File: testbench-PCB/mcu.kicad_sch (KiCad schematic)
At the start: 17 parts, among them J2 AVR-ISP, J3 AVR-JTAG, SW1 SW_Push, U1 ATmega2561-16A, Y1 X322516MLB4SI

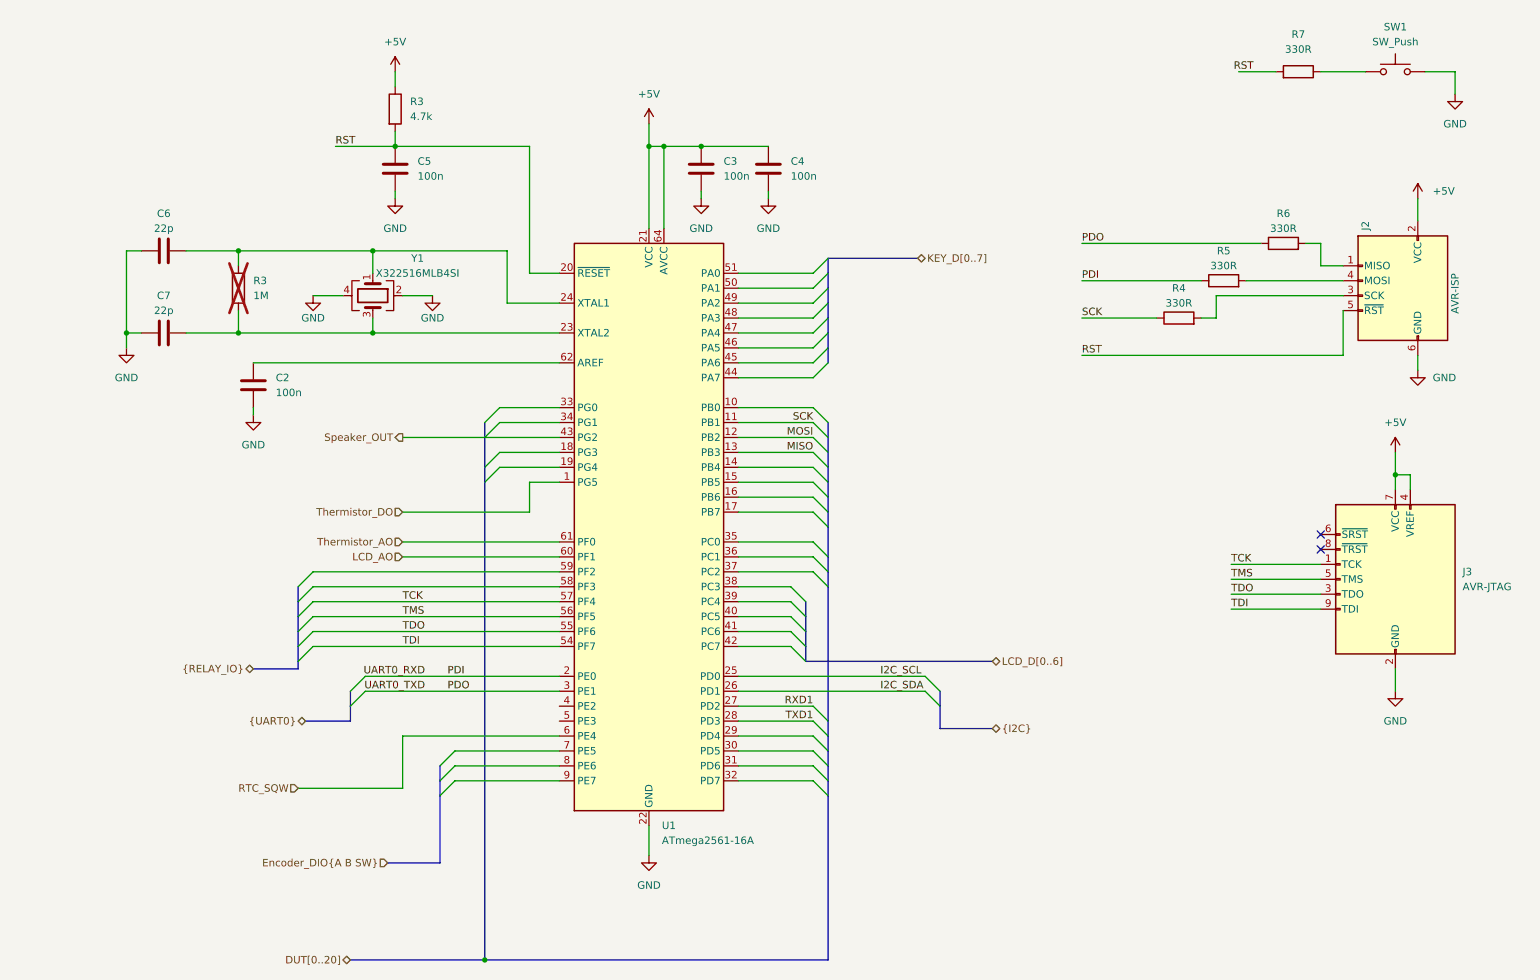
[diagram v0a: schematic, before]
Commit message: Rearanged PCB, updated footprints.
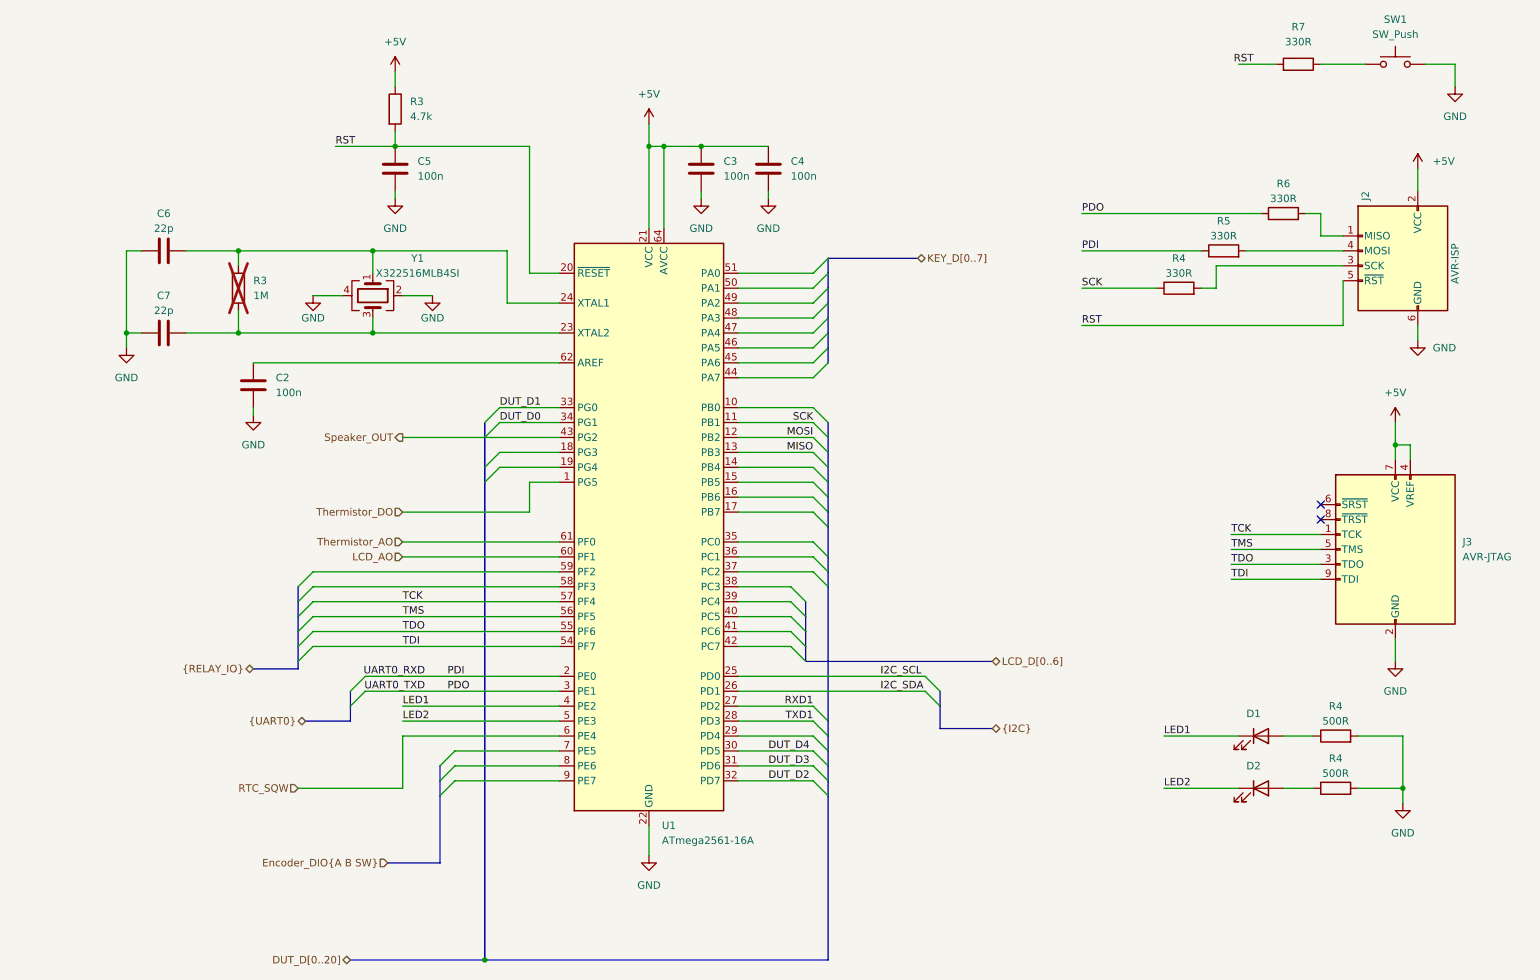
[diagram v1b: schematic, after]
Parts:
- added D1, D2: LED, LED_SMD:LED_0805_2012Metric, symbol Device:LED
- added R4 (x2): 500R, Resistor_SMD:R_0805_2012Metric, symbol Device:R
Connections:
- net GND: now also R4.2, R4.2
- net DUT_D4: now reaches U1.30 (PD5)
- net DUT_D3: now reaches U1.31 (PD6)
- net DUT_D2: now reaches U1.32 (PD7)
- net DUT_D1: now reaches U1.33 (PG0)
- net DUT_D0: now reaches U1.34 (PG1)
- net LED1: now reaches U1.4 (PE2)
- net LED1: now also D1.1 (K)
- net LED2: now reaches U1.5 (PE3)
- net LED2: now also D2.1 (K)
- new net: D1.2 (A), R4.1
- new net: D2.2 (A), R4.1
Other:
- moved on the sheet: J2, J3, R4, R5, R6, R7, SW1

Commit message: Routing the PCB.
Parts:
- removed D1: LED, LED_SMD:LED_0805_2012Metric, symbol Device:LED
- removed R4: 500R, Resistor_SMD:R_0805_2012Metric, symbol Device:R
- added C4: 100n, Capacitor_SMD:C_0805_2012Metric, symbol Device:C
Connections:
- net LED1 is gone; now on net Speaker_OUT: U1.4 (PE2)
- net +5V: now also C4.1
- net DUT_D0: now also U1.37 (PC2); no longer U1.34 (PG1)
- net DUT_D1: now also U1.36 (PC1); no longer U1.33 (PG0)
- net DUT_D2: now also U1.35 (PC0); no longer U1.32 (PD7)
- net DUT_D3: now also U1.34 (PG1); no longer U1.31 (PD6)
- net DUT_D4: now also U1.33 (PG0); no longer U1.30 (PD5)
- net GND: now also C4.2
- net LED2: now also D2.2 (A); no longer D2.1 (K), U1.5 (PE3)
- net Speaker_OUT: no longer U1.43 (PG2)
- net at R4.1: now also D2.1 (K); no longer D2.2 (A)
- net DUT_D17: now reaches U1.10 (PB0)
- net DUT_D16: now reaches U1.14 (PB4)
- net DUT_D15: now reaches U1.15 (PB5)
- net DUT_D14: now reaches U1.16 (PB6)
- net DUT_D13: now reaches U1.17 (PB7)
- net DUT_D12: now reaches U1.18 (PG3)
- net DUT_D11: now reaches U1.19 (PG4)
- net DUT_D9: now reaches U1.29 (PD4)
- net LCD_D0: now reaches U1.38 (PC3)
- net LCD_D1: now reaches U1.39 (PC4)
- net LCD_D2: now reaches U1.40 (PC5)
- net LCD_D3: now reaches U1.41 (PC6)
- net LCD_D4: now reaches U1.42 (PC7)
- net KEY_D0: now reaches U1.44 (PA7)
- net KEY_D1: now reaches U1.45 (PA6)
- net KEY_D2: now reaches U1.46 (PA5)
- net KEY_D3: now reaches U1.47 (PA4)
- net KEY_D4: now reaches U1.48 (PA3)
- net KEY_D5: now reaches U1.49 (PA2)
- net KEY_D6: now reaches U1.50 (PA1)
- net KEY_D7: now reaches U1.51 (PA0)
- net K1-IN: now reaches U1.58 (PF3)
- net K2-IN: now reaches U1.59 (PF2)
- net ENC.A: now reaches U1.7 (PE5)
- net ENC.B: now reaches U1.8 (PE6)
- net ENC.SW: now reaches U1.9 (PE7)
- net MISO renamed DUT_D18
- net MOSI renamed DUT_D19
- net RXD1 renamed DUT_D8
- net SCK renamed DUT_D20
- net TCK renamed K2-NC
- net TDI renamed K2-NO
- net TDO renamed K1-NO
- net TMS renamed K1-NC
- net TXD1 renamed DUT_D7
- new net DUT_D10: U1.30 (PD5)
- new net DUT_D5: U1.32 (PD7)
- new net DUT_D6: U1.31 (PD6)
- new net LCD_D5: U1.43 (PG2)
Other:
- moved on the sheet: C4, D2

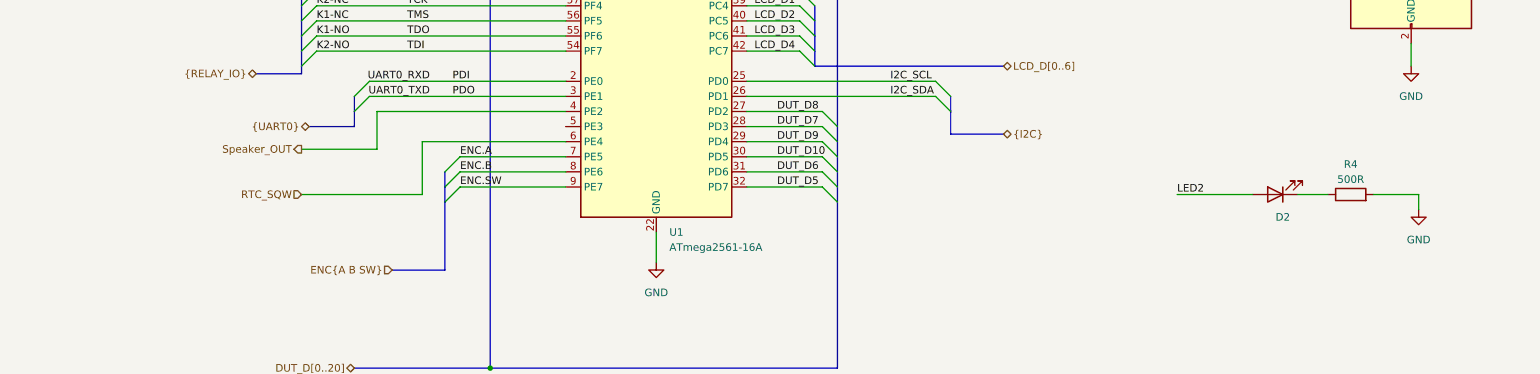
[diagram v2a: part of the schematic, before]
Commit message: Finished PCB routing, added ground plane.
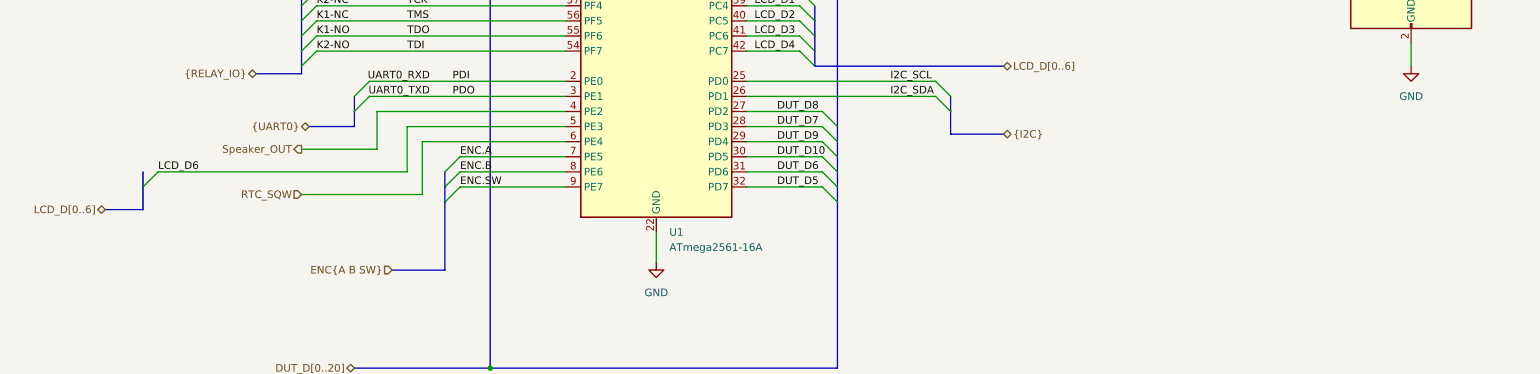
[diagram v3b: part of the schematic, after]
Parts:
- removed D2: LED, LED_SMD:LED_0805_2012Metric, symbol Device:LED
- removed R4: 500R, Resistor_SMD:R_0805_2012Metric, symbol Device:R
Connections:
- net LCD_D6: now reaches U1.5 (PE3)
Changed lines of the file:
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@@
+    (stroke (width 0) (type default))
+  )
+  (bus_entry (at 41.91 153.67) (size 2.54 -2.54)
     (stroke (width 0) (type default))
   )
@@
     (stroke (width 0) (type default))
   )
+  (wire (pts (xy 86.36 143.51) (xy 86.36 151.13))
+    (stroke (width 0) (type default))
+  )
   (wire (pts (xy 104.14 63.5) (xy 81.28 63.5))
     (stroke (width 0) (type default))
@@
     (stroke (width 0) (type default))
   )
+  (wire (pts (xy 113.03 143.51) (xy 86.36 143.51))
+    (stroke (width 0) (type default))
+  )
   (bus (pts (xy 158.75 115.57) (xy 158.75 118.11))
     (stroke (width 0) (type default))
@@
     (stroke (width 0) (type default))
   )
-  (wire (pts (xy 248.92 154.94) (xy 256.54 154.94))
-    (stroke (width 0) (type default))
-  )
   (bus (pts (xy 68.58 128.27) (xy 68.58 130.81))
     (stroke (width 0) (type default))
@@
     (stroke (width 0) (type default))
   )
+  (bus (pts (xy 41.91 153.67) (xy 41.91 157.48))
+    (stroke (width 0) (type default))
+  )
   (wire (pts (xy 259.08 78.74) (xy 259.08 76.2))
     (stroke (width 0) (type default))
@@
     (stroke (width 0) (type default))
   )
-  (wire (pts (xy 256.54 154.94) (xy 256.54 157.48))
-    (stroke (width 0) (type default))
-  )
   (wire (pts (xy 60.96 90.17) (xy 60.96 91.44))
     (stroke (width 0) (type default))
@@
     (stroke (width 0) (type default))
   )
-  (wire (pts (xy 236.22 154.94) (xy 241.3 154.94))
-    (stroke (width 0) (type default))
-  )
   (bus (pts (xy 68.58 125.73) (xy 68.58 128.27))
     (stroke (width 0) (type default))
@@
     (stroke (width 0) (type default))
   )
+  (wire (pts (xy 44.45 151.13) (xy 86.36 151.13))
+    (stroke (width 0) (type default))
+  )
   (bus (pts (xy 88.9 97.79) (xy 88.9 101.6))
     (stroke (width 0) (type default))
@@
     (stroke (width 0) (type default))
   )
+  (bus (pts (xy 41.91 151.13) (xy 41.91 153.67))
+    (stroke (width 0) (type default))
+  )
   (wire (pts (xy 100.33 95.25) (xy 113.03 95.25))
     (stroke (width 0) (type default))
@@
     (stroke (width 0) (type default))
   )
-  (wire (pts (xy 215.9 154.94) (xy 228.6 154.94))
-    (stroke (width 0) (type default))
-  )
   (bus (pts (xy 100.33 95.25) (xy 100.33 100.33))
     (stroke (width 0) (type default))
@@
     (stroke (width 0) (type default))
   )
+  (bus (pts (xy 35.56 157.48) (xy 41.91 157.48))
+    (stroke (width 0) (type default))
+  )
   (bus (pts (xy 158.75 153.67) (xy 158.75 156.21))
     (stroke (width 0) (type default))
@@
   )
   (label "TDO" (at 227.33 116.84 0) (fields_autoplaced)
+    (effects (font (size 1.27 1.27)) (justify left bottom))
+  )
+  (label "LCD_D6" (at 44.45 151.13 0) (fields_autoplaced)
     (effects (font (size 1.27 1.27)) (justify left bottom))
   )
@@
     (effects (font (size 1.27 1.27)) (justify left bottom))
   )
-  (label "LED2" (at 215.9 154.94 0) (fields_autoplaced)
-    (effects (font (size 1.27 1.27)) (justify left bottom))
-  )
   (label "DUT_D18" (at 148.59 97.79 0) (fields_autoplaced)
     (effects (font (size 1.27 1.27)) (justify left bottom))
@@
   )
   (hierarchical_label "{UART0}" (shape bidirectional) (at 69.85 143.51 180) (fields_autoplaced)
+    (effects (font (size 1.27 1.27)) (justify right))
+  )
+  (hierarchical_label "LCD_D[0..6]" (shape bidirectional) (at 35.56 157.48 180) (fields_autoplaced)
     (effects (font (size 1.27 1.27)) (justify right))
   )
@@
         (path "/3ac6901d-218d-4b34-8c4a-bf7c417c33bc/08a6730c-9a7c-47f6-b930-4f7799d77218"
           (reference "#PWR016") (unit 1)
-        )
-      )
-    )
-  )
-  (symbol (lib_id "power:GND") (at 256.54 157.48 0) (unit 1)
-    (in_bom yes) (on_board yes) (dnp no) (fields_autoplaced)
-    (property "Reference" "#PWR044" (at 256.54 163.83 0)
-      (effects (font (size 1.27 1.27)) hide)
-    )
-    (property "Value" "GND" (at 256.54 162.56 0)
-      (effects (font (size 1.27 1.27)))
-    )
-    (property "Footprint" "" (at 256.54 157.48 0)
-      (effects (font (size 1.27 1.27)) hide)
-    )
-    (property "Datasheet" "" (at 256.54 157.48 0)
-      (effects (font (size 1.27 1.27)) hide)
-    )
-    (pin "1")
-    (instances
-      (project "testbench"
-        (path "/3ac6901d-218d-4b34-8c4a-bf7c417c33bc/08a6730c-9a7c-47f6-b930-4f7799d77218"
-          (reference "#PWR044") (unit 1)
-        )
-      )
-    )
-  )
-  (symbol (lib_id "Device:R") (at 245.11 154.94 90) (unit 1)
-    (in_bom yes) (on_board yes) (dnp no)
-    (property "Reference" "R4" (at 245.11 149.86 90)
-      (effects (font (size 1.27 1.27)))
-    )
-    (property "Value" "500R" (at 245.11 152.4 90)
-      (effects (font (size 1.27 1.27)))
-    )
-    (property "Footprint" "Resistor_SMD:R_0805_2012Metric" (at 245.11 156.718 90)
-      (effects (font (size 1.27 1.27)) hide)
-    )
-    (property "Datasheet" "~" (at 245.11 154.94 0)
-      (effects (font (size 1.27 1.27)) hide)
-    )
-    (pin "1")
-    (pin "2")
-    (instances
-      (project "testbench"
-        (path "/3ac6901d-218d-4b34-8c4a-bf7c417c33bc"
-          (reference "R4") (unit 1)
-        )
-        (path "/3ac6901d-218d-4b34-8c4a-bf7c417c33bc/08a6730c-9a7c-47f6-b930-4f7799d77218"
-          (reference "R16") (unit 1)
         )
       )
@@
         )
       )
-    )
-  )
-  (symbol (lib_id "Device:LED") (at 232.41 154.94 180) (unit 1)
-    (in_bom yes) (on_board yes) (dnp no)
-    (property "Reference" "D2" (at 233.68 158.75 0)
-      (effects (font (size 1.27 1.27)))
-    )
-    (property "Value" "LED" (at 233.9975 158.75 0)
-      (effects (font (size 1.27 1.27)) hide)
-    )
-    (property "Footprint" "LED_SMD:LED_0805_2012Metric" (at 232.41 154.94 0)
-      (effects (font (size 1.27 1.27)) hide)
-    )
-    (property "Datasheet" "~" (at 232.41 154.94 0)
-      (effects (font (size 1.27 1.27)) hide)
-    )
-    (pin "1")
-    (pin "2")
-    (instances
-      (project "testbench"
-        (path "/3ac6901d-218d-4b34-8c4a-bf7c417c33bc/08a6730c-9a7c-47f6-b930-4f7799d77218"
-          (reference "D2") (unit 1)
-        )
-      )

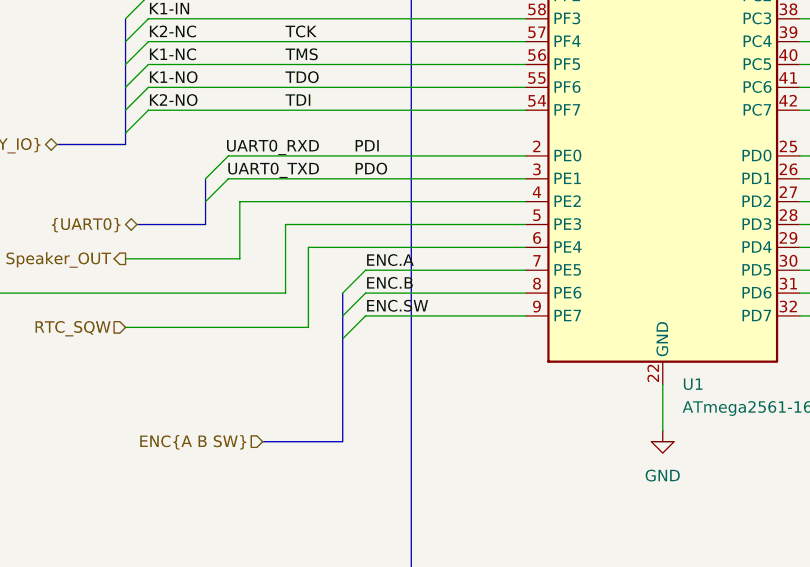
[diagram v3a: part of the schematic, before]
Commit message: Changed encoder module pinout, added labels.
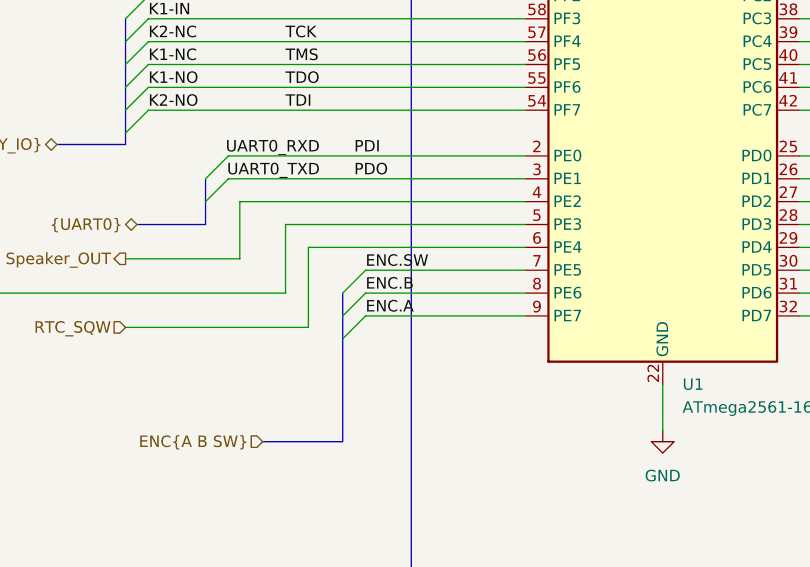
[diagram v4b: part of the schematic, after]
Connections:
- net ENC.A: now also U1.9 (PE7); no longer U1.7 (PE5)
- net ENC.SW: now also U1.7 (PE5); no longer U1.9 (PE7)
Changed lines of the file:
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@@
     (effects (font (size 1.27 1.27)) (justify left bottom))
   )
-  (label "ENC.A" (at 95.25 148.59 0) (fields_autoplaced)
+  (label "ENC.SW" (at 95.25 148.59 0) (fields_autoplaced)
     (effects (font (size 1.27 1.27)) (justify left bottom))
   )
@@
     (effects (font (size 1.27 1.27)) (justify left bottom))
   )
-  (label "ENC.SW" (at 95.25 153.67 0) (fields_autoplaced)
+  (label "ENC.A" (at 95.25 153.67 0) (fields_autoplaced)
     (effects (font (size 1.27 1.27)) (justify left bottom))
   )
